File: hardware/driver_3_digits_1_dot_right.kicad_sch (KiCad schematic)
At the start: 11 parts, among them U5 HV5622PG

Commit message: Fix DRC errors.
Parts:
- DOT2: footprint nixies-us_IN-3 -> nixies-us:nixies-us-IN-3
- N4, N5, N6: footprint nixies-us_IN-14 -> nixies-us:nixies-us-IN-14
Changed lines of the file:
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@@
 			)
 		)
-		(property "Footprint" "nixies-us_IN-3"
+		(property "Footprint" "nixies-us:nixies-us-IN-3"
 			(at 161.798 55.88 0)
 			(effects
@@
 			)
 		)
-		(property "Footprint" "nixies-us_IN-14"
+		(property "Footprint" "nixies-us:nixies-us-IN-14"
 			(at 120.142 41.91 0)
 			(effects
@@
 			)
 		)
-		(property "Footprint" "nixies-us_IN-14"
+		(property "Footprint" "nixies-us:nixies-us-IN-14"
 			(at 121.412 82.55 0)
 			(effects
@@
 			)
 		)
-		(property "Footprint" "nixies-us_IN-14"
+		(property "Footprint" "nixies-us:nixies-us-IN-14"
 			(at 122.682 121.92 0)
 			(effects

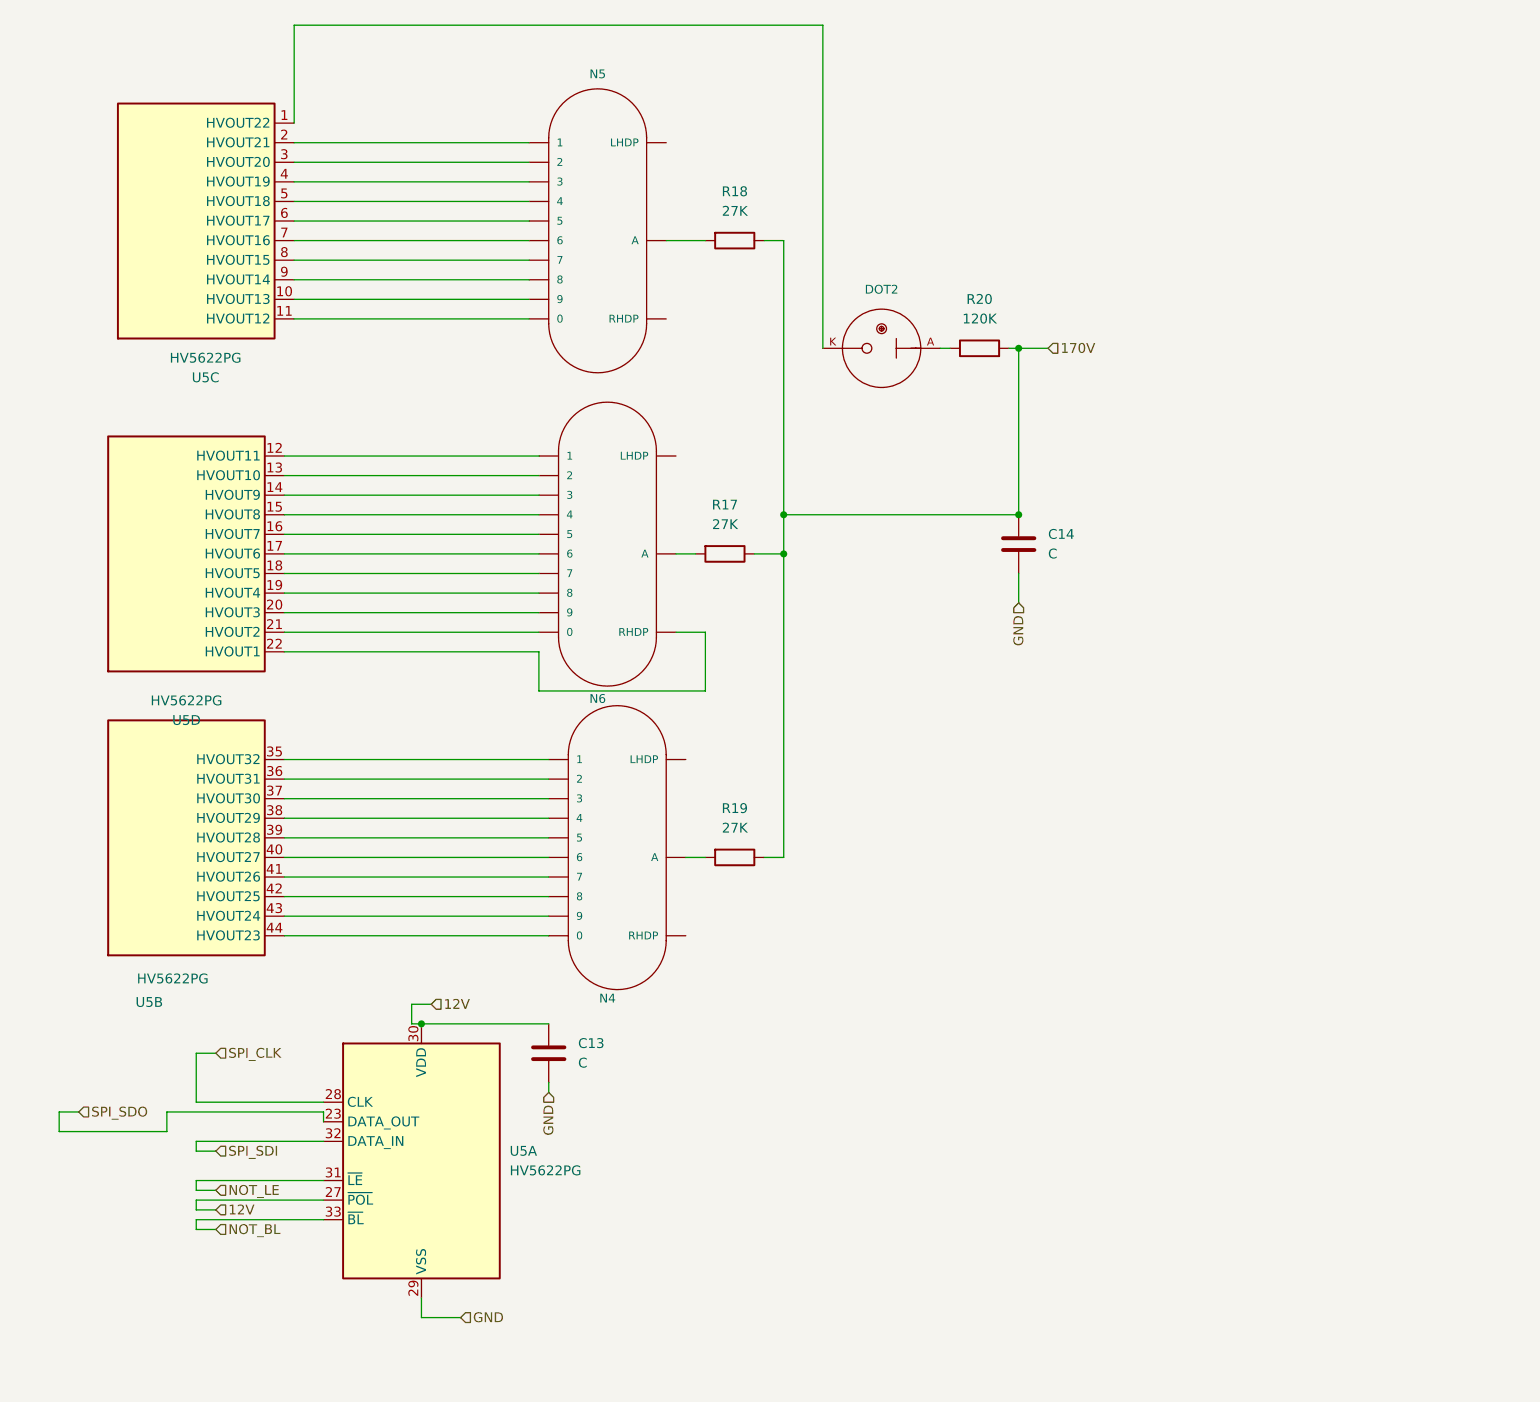
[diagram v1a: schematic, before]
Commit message: Fix most of ERC on schema. Add missing wire on RV1. Add PWR_FLG on GND to avoid error. Add resistor for unused SPI_OUT of HV5622. Add PTC on 3v3 supply.
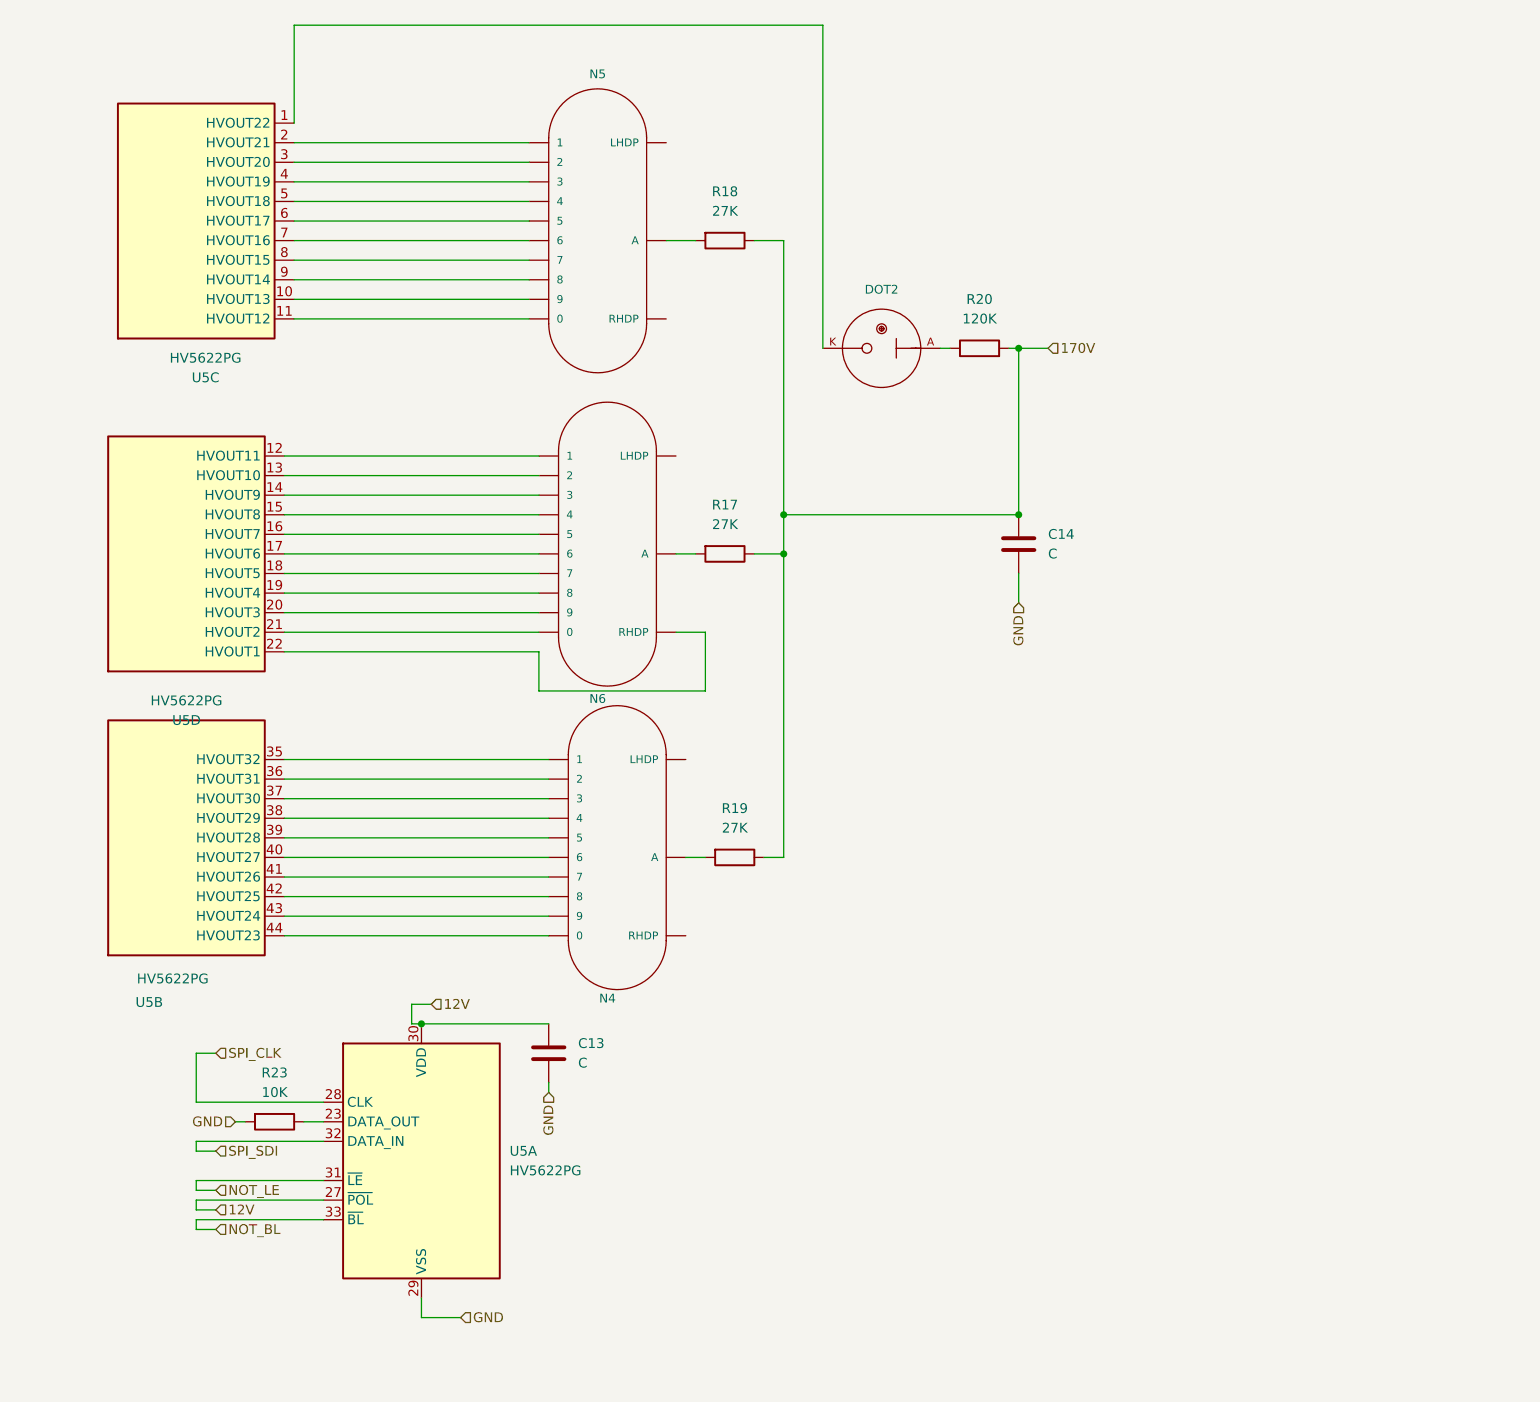
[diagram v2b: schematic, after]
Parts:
- added R23: 10K, Resistor_SMD:R_0805_2012Metric, symbol Device:R
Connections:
- net GND: now also R23.2
- net SPI_SDO: no longer names the net of U5.23 (DATA_OUT)
- net SPI_SDO: now also R23.1
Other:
- moved on the sheet: R18
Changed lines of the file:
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@@
-	(wire
-		(pts
-			(xy 50.8 163.83) (xy 50.8 161.29)
-		)
-		(stroke
-			(width 0)
-			(type default)
-		)
-	)
 	(wire
 		(pts
@@
 	(wire
 		(pts
+			(xy 82.55 162.56) (xy 85.09 162.56)
+		)
+		(stroke
+			(width 0)
+			(type default)
+		)
+	)
+	(wire
+		(pts
 			(xy 81.28 43.18) (xy 111.76 43.18)
 		)
@@
 	(wire
 		(pts
-			(xy 85.09 162.56) (xy 85.09 161.29)
+			(xy 73.66 162.56) (xy 74.93 162.56)
 		)
 		(stroke
@@
 	(wire
 		(pts
-			(xy 64.77 163.83) (xy 50.8 163.83)
-		)
-		(stroke
-			(width 0)
-			(type default)
-		)
-	)
-	(wire
-		(pts
 			(xy 80.01 118.11) (xy 114.3 118.11)
 		)
@@
 	(wire
 		(pts
-			(xy 85.09 161.29) (xy 64.77 161.29)
-		)
-		(stroke
-			(width 0)
-			(type default)
-		)
-	)
-	(wire
-		(pts
 			(xy 130.81 88.9) (xy 133.35 88.9)
 		)
@@
 	(wire
 		(pts
-			(xy 64.77 161.29) (xy 64.77 163.83)
-		)
-		(stroke
-			(width 0)
-			(type default)
-		)
-	)
-	(wire
-		(pts
 			(xy 68.58 175.26) (xy 85.09 175.26)
 		)
@@
 	(wire
 		(pts
-			(xy 50.8 161.29) (xy 53.34 161.29)
-		)
-		(stroke
-			(width 0)
-			(type default)
-		)
-	)
-	(wire
-		(pts
 			(xy 173.99 62.23) (xy 175.26 62.23)
 		)
@@
 	(wire
 		(pts
-			(xy 129.54 48.26) (xy 134.62 48.26)
+			(xy 129.54 48.26) (xy 133.35 48.26)
 		)
 		(stroke
@@
 	(wire
 		(pts
-			(xy 142.24 48.26) (xy 144.78 48.26)
+			(xy 140.97 48.26) (xy 144.78 48.26)
 		)
 		(stroke
@@
 		)
 	)
-	(hierarchical_label "SPI_SDO"
-		(shape input)
-		(at 53.34 161.29 0)
-		(effects
-			(font
-				(size 1.27 1.27)
-			)
-			(justify left)
-		)
-	)
 	(hierarchical_label "NOT_BL"
 		(shape input)
@@
 			)
 			(justify left)
+		)
+	)
+	(hierarchical_label "GND"
+		(shape input)
+		(at 73.66 162.56 180)
+		(effects
+			(font
+				(size 1.27 1.27)
+			)
+			(justify right)
 		)
 	)
@@
 	(symbol
 		(lib_id "Device:R")
-		(at 138.43 48.26 270)
+		(at 137.16 48.26 270)
 		(unit 1)
 		(exclude_from_sim no)
@@
 		(fields_autoplaced yes)
 		(property "Reference" "R18"
-			(at 138.43 41.91 90)
+			(at 137.16 41.91 90)
 			(effects
 				(font
@@
 		)
 		(property "Value" "27K"
-			(at 138.43 44.45 90)
+			(at 137.16 44.45 90)
 			(effects
 				(font
@@
 		)
 		(property "Footprint" "Resistor_SMD:R_1206_3216Metric"
-			(at 138.43 46.482 90)
+			(at 137.16 46.482 90)
 			(effects
 				(font
@@
 		)
 		(property "Datasheet" "~"
-			(at 138.43 48.26 0)
+			(at 137.16 48.26 0)
 			(effects
 				(font
@@
 		)
 		(property "Description" "Resistor"
-			(at 138.43 48.26 0)
+			(at 137.16 48.26 0)
 			(effects
 				(font
@@
 					(unit 1)
 				)
+			)
+		)
+	)
+	(symbol
+		(lib_id "Device:R")
+		(at 78.74 162.56 270)
+		(unit 1)
+		(exclude_from_sim no)
+		(in_bom yes)
+		(on_board yes)
+		(dnp no)
+		(fields_autoplaced yes)
+		(property "Reference" "R23"
+			(at 78.74 156.21 90)
+			(effects
+				(font
+					(size 1.27 1.27)
+				)
+			)
+		)
+		(property "Value" "10K"
+			(at 78.74 158.75 90)
+			(effects
+				(font
+					(size 1.27 1.27)
+				)
+			)
+		)
+		(property "Footprint" "Resistor_SMD:R_0805_2012Metric"
+			(at 78.74 160.782 90)
+			(effects
+				(font
+					(size 1.27 1.27)
+				)
+				(hide yes)
+			)
+		)
+		(property "Datasheet" "~"
+			(at 78.74 162.56 0)
+			(effects
+				(font
+					(size 1.27 1.27)
+				)
+				(hide yes)
+			)
+		)
+		(property "Description" "Resistor"
+			(at 78.74 162.56 0)
+			(effects
+				(font
+					(size 1.27 1.27)
+				)
+				(hide yes)
+			)
+		)
+		(pin "2"
+		)
+		(pin "1"
+		)
+		(instances
+			(project "nixie_clock"
+				(path "/90430e5f-7049-4de8-b92d-f897c4a89819/fe830805-1f17-45c2-a3b2-c398af349661"
+					(reference "R23")
+					(unit 1)
+				)

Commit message: Remove HV capacitor for Nixies. Add more LCSC references.
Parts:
- removed C14: C, Capacitor_SMD:C_1206_3216Metric, symbol Device:C
- C13: value C -> 100nF
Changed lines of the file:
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@@
-	)
-	(junction
-		(at 175.26 83.82)
-		(diameter 0)
-		(color 0 0 0 0)
 	)
 	(junction
@@
 		(pts
 			(xy 81.28 35.56) (xy 111.76 35.56)
-		)
-		(stroke
-			(width 0)
-			(type default)
-		)
-	)
-	(wire
-		(pts
-			(xy 175.26 91.44) (xy 175.26 95.25)
 		)
 		(stroke
@@
 			)
 			(justify left)
-		)
-	)
-	(hierarchical_label "GND"
-		(shape input)
-		(at 175.26 95.25 270)
-		(effects
-			(font
-				(size 1.27 1.27)
-			)
-			(justify right)
 		)
 	)
@@
 			)
 		)
-		(property "Value" "C"
+		(property "Value" "100nF"
 			(at 118.11 154.9399 0)
 			(effects
@@
 				)
 			)
-		)
-	)
-	(symbol
-		(lib_id "Device:C")
-		(at 175.26 87.63 0)
-		(unit 1)
-		(exclude_from_sim no)
-		(in_bom yes)
-		(on_board yes)
-		(dnp no)
-		(fields_autoplaced yes)
-		(property "Reference" "C14"
-			(at 179.07 86.3599 0)
-			(effects
-				(font
-					(size 1.27 1.27)
-				)
-				(justify left)
-			)
-		)
-		(property "Value" "C"
-			(at 179.07 88.8999 0)
-			(effects
-				(font
-					(size 1.27 1.27)
-				)
-				(justify left)
-			)
-		)
-		(property "Footprint" "Capacitor_SMD:C_1206_3216Metric"
-			(at 176.2252 91.44 0)
-			(effects
-				(font
-					(size 1.27 1.27)
-				)
-				(hide yes)
-			)
-		)
-		(property "Datasheet" "~"
-			(at 175.26 87.63 0)
-			(effects
-				(font
-					(size 1.27 1.27)
-				)
-				(hide yes)
-			)
-		)
-		(property "Description" "Unpolarized capacitor"
-			(at 175.26 87.63 0)
-			(effects
-				(font
-					(size 1.27 1.27)
-				)
-				(hide yes)
-			)
-		)
-		(pin "2"
-		)
-		(pin "1"
-		)
-		(instances
-			(project "nixie_clock"
-				(path "/90430e5f-7049-4de8-b92d-f897c4a89819/fe830805-1f17-45c2-a3b2-c398af349661"
-					(reference "C14")
-					(unit 1)
-				)
-			)
